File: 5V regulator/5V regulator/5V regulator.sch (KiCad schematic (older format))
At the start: 8 parts, among them J1 9V Vhod, J2 5V Izhod, U1 LM7805_TO220

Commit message: 5v regulator pcb
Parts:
- J1, J2: footprint w_conn_screw:mors_2p -> TerminalBlock:TerminalBlock_bornier-2_P5.08mm
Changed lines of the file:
@@
 F 0 "J2" H 6500 3700 50  0000 L CNN
 F 1 "5V Izhod" H 6450 3400 50  0000 L CNN
-F 2 "w_conn_screw:mors_2p" H 6500 3600 50  0001 C CNN
+F 2 "TerminalBlock:TerminalBlock_bornier-2_P5.08mm" H 6500 3600 50  0001 C CNN
 F 3 "~" H 6500 3600 50  0001 C CNN
 	1    6500 3600
@@
 F 0 "J1" H 3650 3500 50  0000 C CNN
 F 1 "9V Vhod" H 3700 3800 50  0000 C CNN
-F 2 "w_conn_screw:mors_2p" H 3650 3700 50  0001 C CNN
+F 2 "TerminalBlock:TerminalBlock_bornier-2_P5.08mm" H 3650 3700 50  0001 C CNN
 F 3 "~" H 3650 3700 50  0001 C CNN
 	1    3650 3700

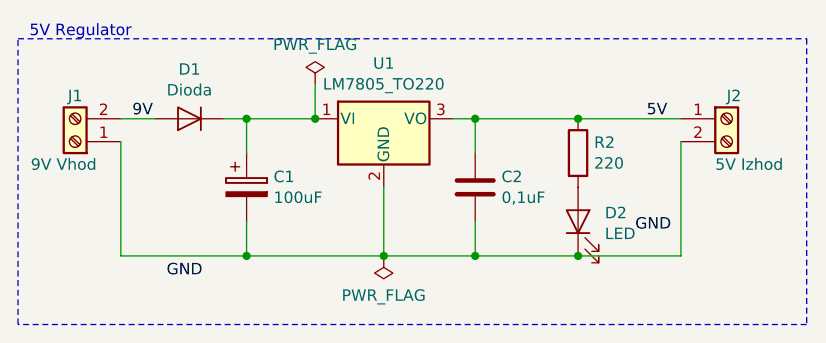
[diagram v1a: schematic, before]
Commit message: updated 5v regulator
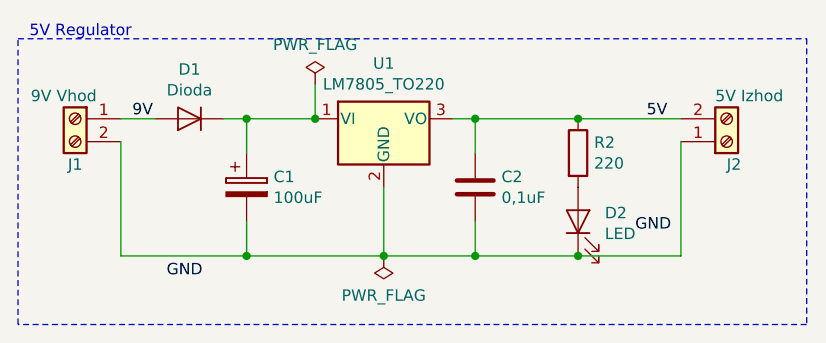
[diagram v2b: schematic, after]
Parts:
- C2: footprint Capacitors_THT:C_Rect_L7.0mm_W2.5mm_P5.00mm -> Capacitor_THT:C_Disc_D10.0mm_W2.5mm_P5.00mm
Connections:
- net 5V: now also J2.2 (Pin_2); no longer J2.1 (Pin_1)
- net 9V: now also J1.1 (Pin_1); no longer J1.2 (Pin_2)
- net at C1.2, C2.2, D2.1 (K)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: now also J1.2 (Pin_2), J2.1 (Pin_1); no longer J1.1 (Pin_1), J2.2 (Pin_2)
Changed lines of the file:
@@
 L Connector:Screw_Terminal_01x02 J2
 U 1 1 5DC2B5ED
-P 6500 3600
-F 0 "J2" H 6500 3700 50  0000 L CNN
-F 1 "5V Izhod" H 6450 3400 50  0000 L CNN
-F 2 "TerminalBlock:TerminalBlock_bornier-2_P5.08mm" H 6500 3600 50  0001 C CNN
-F 3 "~" H 6500 3600 50  0001 C CNN
-	1    6500 3600
-	1    0    0    -1
+P 6500 3700
+F 0 "J2" H 6500 3800 50  0000 L CNN
+F 1 "5V Izhod" H 6450 3500 50  0000 L CNN
+F 2 "TerminalBlock:TerminalBlock_bornier-2_P5.08mm" H 6500 3700 50  0001 C CNN
+F 3 "~" H 6500 3700 50  0001 C CNN
+	1    6500 3700
+	1    0    0    1
 $EndComp
 $Comp
 L Connector:Screw_Terminal_01x02 J1
 U 1 1 5DC2B6DA
-P 3650 3700
-F 0 "J1" H 3650 3500 50  0000 C CNN
-F 1 "9V Vhod" H 3700 3800 50  0000 C CNN
-F 2 "TerminalBlock:TerminalBlock_bornier-2_P5.08mm" H 3650 3700 50  0001 C CNN
-F 3 "~" H 3650 3700 50  0001 C CNN
-	1    3650 3700
-	-1   0    0    1
+P 3650 3600
+F 0 "J1" H 3650 3400 50  0000 C CNN
+F 1 "9V Vhod" H 3700 3700 50  0000 C CNN
+F 2 "TerminalBlock:TerminalBlock_bornier-2_P5.08mm" H 3650 3600 50  0001 C CNN
+F 3 "~" H 3650 3600 50  0001 C CNN
+	1    3650 3600
+	-1   0    0    -1
 $EndComp
 Text Label 3900 3600 0    50   ~ 0
@@
 F 0 "C2" H 5515 3946 50  0000 L CNN
 F 1 "0,1uF" H 5515 3855 50  0000 L CNN
-F 2 "Capacitors_THT:C_Rect_L7.0mm_W2.5mm_P5.00mm" H 5438 3750 50  0001 C CNN
+F 2 "Capacitor_THT:C_Disc_D10.0mm_W2.5mm_P5.00mm" H 5438 3750 50  0001 C CNN
 F 3 "~" H 5400 3900 50  0001 C CNN
 	1    5400 3900
@@
 	1    0    0    -1
 $EndComp
-Connection ~ 5850 3600
-Wire Wire Line
-	5850 3600 6300 3600
 $Comp
 L Device:LED D2
@@
 Wire Wire Line
 	5000 4200 4400 4200
-Wire Wire Line
-	3850 3700 3850 4200
 Connection ~ 5000 4200
 Wire Wire Line
@@
 Wire Wire Line
 	5400 4200 5000 4200
+Wire Wire Line
+	3850 3700 3850 4200
+Wire Wire Line
+	6300 3600 5850 3600
+Connection ~ 5850 3600
 $EndSCHEMATC
